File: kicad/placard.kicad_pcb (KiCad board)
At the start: 4 copper layers, 290 x 215 mm, 187 parts, among them J10 Slot 2, J11 Slot 3, J12 Slot 4, J13 USB4125-GF-A, J2 SNES pad, J3 SNES pad, J4 SD (SPI), J5 PS/2 kbd + mouse, J6 3.5 mm, J7 VGA, J8 Molex 87715-9106, J9 Slot 1, K1 J1071CS5VDC.36, SW1 ANT11TFHQE, SW2 PTS645VL58-2 LFS, U1 ATF22V10C-7PX, U10 ATF22V10C-7PX, U11 ATF22V10C-7PX, U12 ATF22V10C-7PX, U13 ATF22V10C-7PX, U14 ATF22V10C-7PX, U15 ATF22V10C-7PX, U16 ATF22V10C-7PX, U17 ATF22V10C-7PX, U18 SN74F377AN, U19 SN74F377AN, U2 ATF22V10C-7PX, U20 SN74F377AN, U21 SN74F377AN, U22 SN74F377AN, U23 CD74HCT377E, U25 CD74ACT273E, U26 SN74F541N, U27 SN74F541N, U29 SN74F541N, U3 ATF22V10C-7PX, U31 AS7C256C-15PCN, U32 AS7C256C-15PCN, U35 ATF22V10C-7PX, U36 SN74HCT574N, U38 ATF22V10C-7PX, U4 ATF22V10C-7PX, U40 MCP1700-3302E/TO, U42 ATF22V10C-7PX, U5 ATF22V10C-7PX, U6 ATF22V10C-7PX, U7 ATF22V10C-7PX, U8 ATF22V10C-7PX, U9 ATF22V10C-7PX, X1 25.175 MHz

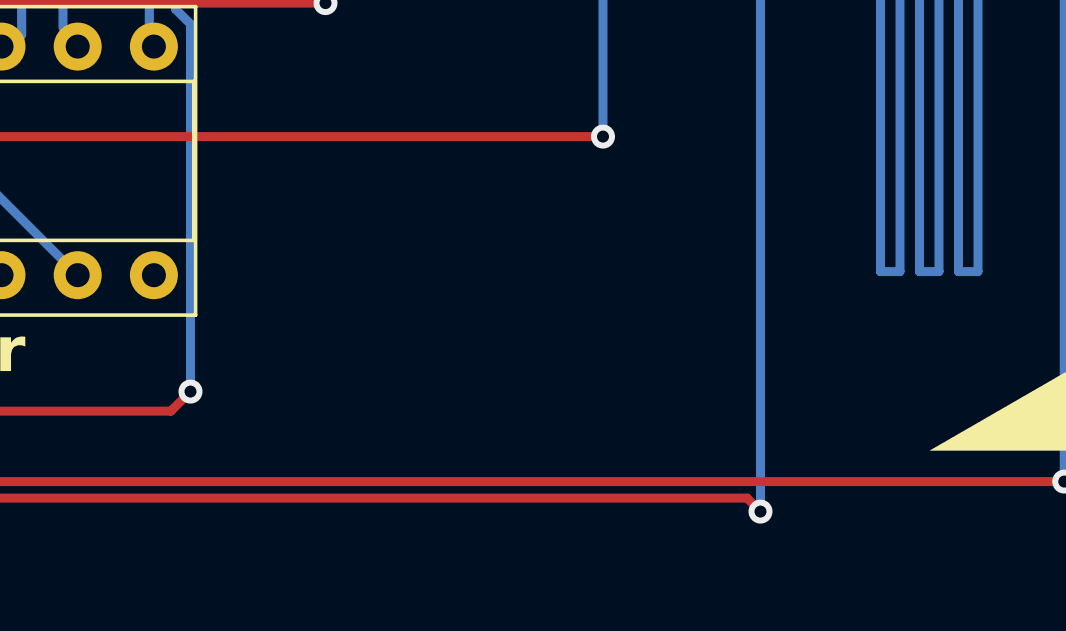
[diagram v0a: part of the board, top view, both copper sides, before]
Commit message: Boards rev A with part numbers PLC-1001/1002/1003 and an S/N box
Silk block on each board (main front by the logo, carts on side B under the
title): PLC-100x REV A, an S/N label and a 17 x 5.5 mm box for a sticker or
paint pen. Board title blocks rev A with the part numbers; schematic title
blocks rev A with PCB/assembly numbers (gen_kicad_schematic.py); BOM bare-PCB
lines carry PLC-100x rev A and assemblies PLC-200x (gen_bom.py).

Co-Authored-By: Claude Opus 5.5 <noreply@anthropic.com>
Claude-Session: https://claude.ai/code/session_01DnW5SVDcRaZyJAhMGzz1W1
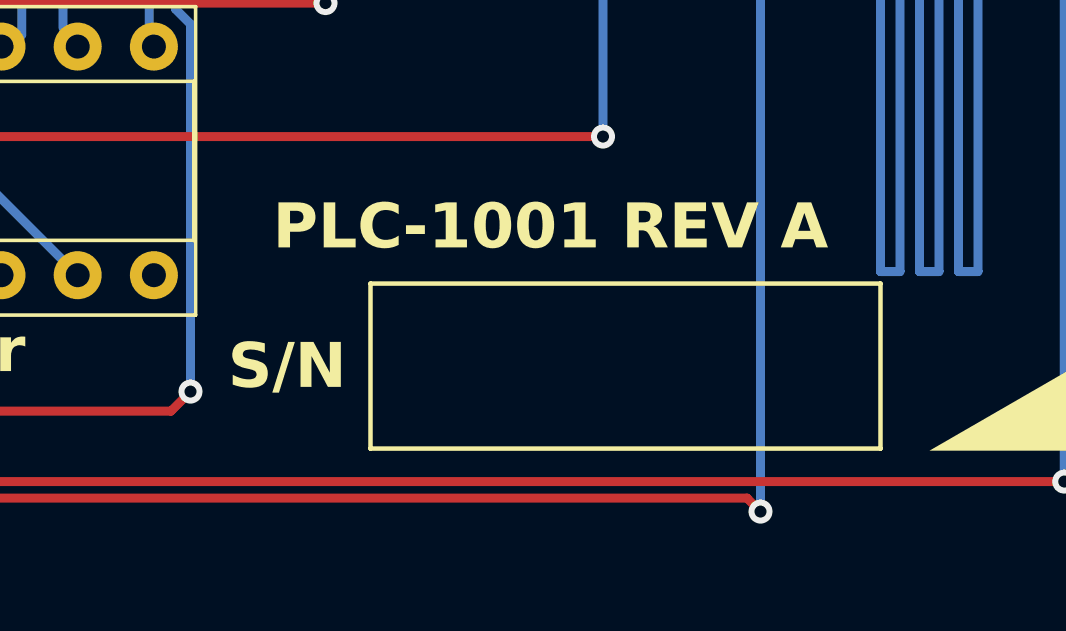
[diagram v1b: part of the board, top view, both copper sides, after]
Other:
- board text added: "PLC-1001 REV A"
- board text added: "S/N"
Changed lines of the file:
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@@
 		(title "Placard")
 		(date "2026-10-29")
-		(rev "0")
+		(rev "A")
+		(comment 1 "PCB PLC-1001, assembly PLC-2001")
 	)
 	(layers
@@
 		(layer "Edge.Cuts")
 	)
+	(gr_text "PLC-1001 REV A"
+		(at 285 250.5 0)
+		(layer "F.SilkS")
+		(effects
+			(font
+				(size 1.5 1.5)
+				(thickness 0.3)
+				(bold yes)
+			)
+		)
+	)
+	(gr_text "S/N"
+		(at 278.2 255.15 0)
+		(layer "F.SilkS")
+		(effects
+			(font
+				(size 1.5 1.5)
+				(thickness 0.3)
+				(bold yes)
+			)
+			(justify right)
+		)
+	)
+	(gr_rect
+		(start 279 252.4)
+		(end 296 257.9)
+		(stroke
+			(width 0.15)
+			(type solid)
+		)
+		(fill no)
+		(layer "F.SilkS")
+	)
 	(gr_text "74F377"
